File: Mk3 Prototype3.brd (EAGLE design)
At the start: 121.6 x 70 mm, 152 parts, among them IC1 TPD3E001DRL, IC2 TPS62082, IC3 STM32F401V, IC4 BQ24092, IC6 CC3100MOD, IC7 BQ2970, IC8 LSM6DS3, IC9 LIS3MDL, J1 ZX62-AB-5PA(11), J2 ER-CON50HT-1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

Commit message: Rework entier power section layout on schematic
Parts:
- JP3: value (none) -> JST PH 2mm
- R32: value DNP (0) -> DNP (0603/0R/5%)
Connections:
- net N$16 renamed VABT_SWTICHED
- net N$57 renamed VBAT_NEG
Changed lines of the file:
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@@
 <attribute name="FARNELL" value="1217769" x="16.2" y="24.8" size="1.778" layer="27" rot="R270" display="off"/>
 </element>
-<element name="JP3" library="TiLDA Mk3 Parts" package="JST-2-SMD" value="" x="47" y="58.8" smashed="yes" rot="MR0">
+<element name="JP3" library="TiLDA Mk3 Parts" package="JST-2-SMD" value="JST PH 2mm" x="47" y="58.8" smashed="yes" rot="MR0">
 <attribute name="NAME" x="48.17" y="61.97" size="1.016" layer="26" font="vector" ratio="14" rot="MR0"/>
 <attribute name="VALUE" x="48.27" y="58.8" size="0.4064" layer="28" rot="MR0"/>
@@
 </element>
 <element name="U2" library="TiLDA Mk3 Parts" package="ER-TFT024-3" value="ER-TFT024-3" x="35.2" y="19.6"/>
-<element name="R32" library="TiLDA Mk3 Parts" package="C0603K-SMALL" value="DNP (0)" x="49.6" y="52.2" smashed="yes" rot="MR90">
+<element name="R32" library="TiLDA Mk3 Parts" package="C0603K-SMALL" value="DNP (0603/0R/5%)" x="49.6" y="52.2" smashed="yes" rot="MR90">
 <attribute name="NAME" x="47.95" y="50.1" size="1.016" layer="26" ratio="14" rot="MR90"/>
 <attribute name="VALUE" x="47.95" y="51.4" size="1.016" layer="28" rot="MR90"/>
@@
 <wire x1="52.2" y1="54.725" x2="52.2" y2="54.625" width="0.2" layer="16"/>
 </signal>
-<signal name="N$57">
+<signal name="VBAT_NEG">
 <contactref element="JP3" pad="1"/>
 <contactref element="IC7" pad="4"/>
@@
 <wire x1="46.92605" y1="24.8" x2="52.67395" y2="24.8" width="0.2" layer="16"/>
 </signal>
-<signal name="N$16">
+<signal name="VABT_SWTICHED">
 <contactref element="Q2" pad="3"/>
 <contactref element="Q1" pad="6"/>
@@
 <wire x1="24.999025" y1="44.171975" x2="23.47" y2="45.701" width="0.2" layer="16"/>
 </signal>
+<signal name="FRAME1">
+</signal>
 </signals>

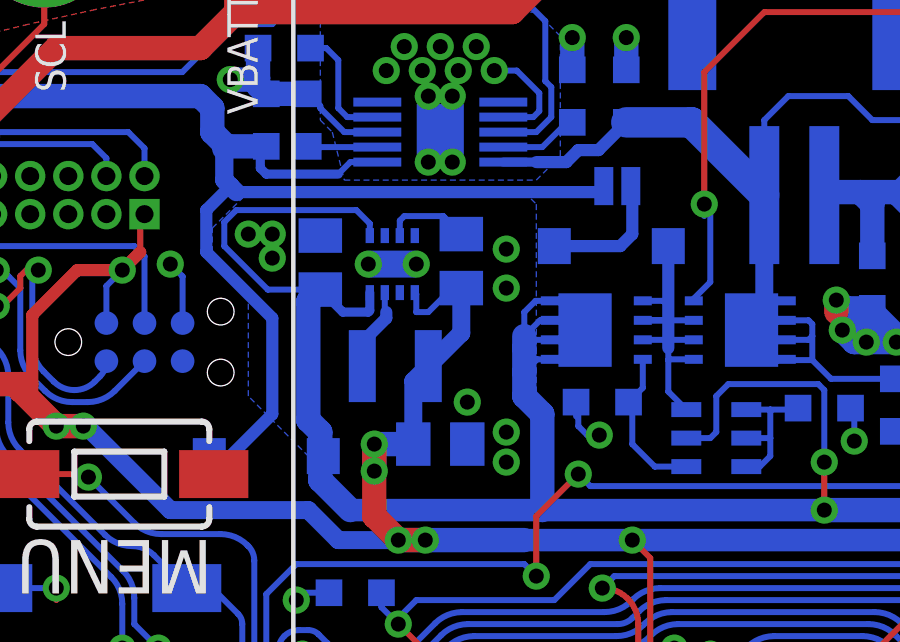
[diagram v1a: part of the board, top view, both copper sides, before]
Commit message: changing 4R7 -> 12R, more schematic tidying
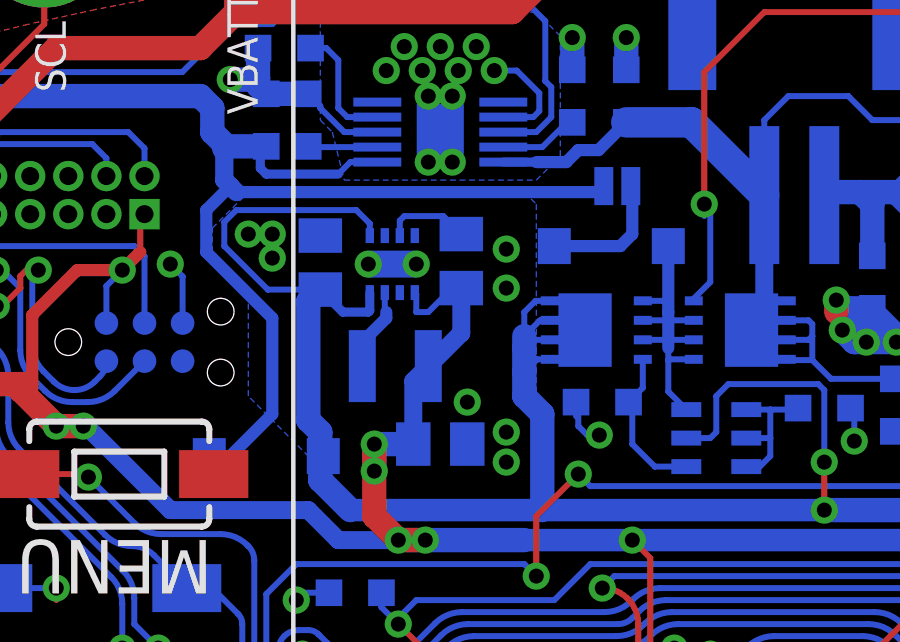
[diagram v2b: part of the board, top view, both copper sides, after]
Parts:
- R11: value DNP / 0603/100K/5% -> DNP
- R44, R47, R48, R49: value 0603/4R7/5% -> 0603/12R/5%
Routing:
- net VABT_SWTICHED: track 13.3 -> 12.5 mm
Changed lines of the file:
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@@
 <attribute name="NAME" x="29.411" y="15.9015" size="1.016" layer="26" font="vector" ratio="14" rot="MR180"/>
 </element>
-<element name="R11" library="TiLDA Mk3 Parts" package="C0603K-SMALL" value="DNP / 0603/100K/5%" x="31.5" y="10.65" smashed="yes" rot="MR0">
+<element name="R11" library="TiLDA Mk3 Parts" package="C0603K-SMALL" value="DNP" x="31.5" y="10.65" smashed="yes" rot="MR0">
 <attribute name="NAME" x="30.111" y="9.9515" size="1.016" layer="26" font="vector" ratio="14" rot="MR180"/>
 <variant name="L4" populate="no"/>
@@
 <variant name="L4" populate="no"/>
 </element>
-<element name="R47" library="TiLDA Mk3 Parts" package="C0603K-SMALL" value="0603/4R7/5%" x="69.6" y="59.2" smashed="yes" rot="MR270">
+<element name="R47" library="TiLDA Mk3 Parts" package="C0603K-SMALL" value="0603/12R/5%" x="69.6" y="59.2" smashed="yes" rot="MR270">
 <attribute name="NAME" x="69.05" y="54.8" size="1.016" layer="26" font="vector" ratio="14" rot="MR90"/>
 <attribute name="FARNELL" value="9331280" x="69.6" y="59.2" size="1.778" layer="28" rot="MR270" display="off"/>
 <attribute name="FARNELL_REEL" value="2130678" x="69.6" y="59.2" size="1.778" layer="28" rot="MR270" display="off"/>
 </element>
-<element name="R48" library="TiLDA Mk3 Parts" package="C0603K-SMALL" value="0603/4R7/5%" x="71.2" y="59.2" smashed="yes" rot="MR270">
+<element name="R48" library="TiLDA Mk3 Parts" package="C0603K-SMALL" value="0603/12R/5%" x="71.2" y="59.2" smashed="yes" rot="MR270">
 <attribute name="NAME" x="70.65" y="54.8" size="1.016" layer="26" font="vector" ratio="14" rot="MR90"/>
 <attribute name="FARNELL" value="9331280" x="71.2" y="59.2" size="1.778" layer="28" rot="MR270" display="off"/>
 <attribute name="FARNELL_REEL" value="2130678" x="71.2" y="59.2" size="1.778" layer="28" rot="MR270" display="off"/>
 </element>
-<element name="R49" library="TiLDA Mk3 Parts" package="C0603K-SMALL" value="0603/4R7/5%" x="72.8" y="59.2" smashed="yes" rot="MR270">
+<element name="R49" library="TiLDA Mk3 Parts" package="C0603K-SMALL" value="0603/12R/5%" x="72.8" y="59.2" smashed="yes" rot="MR270">
 <attribute name="NAME" x="72.25" y="54.8" size="1.016" layer="26" font="vector" ratio="14" rot="MR90"/>
 <attribute name="FARNELL" value="9331280" x="72.8" y="59.2" size="1.778" layer="28" rot="MR270" display="off"/>
@@
 <attribute name="NAME" x="61.895" y="54.0524" size="1.016" layer="26" font="vector" ratio="14" rot="MR90"/>
 </element>
-<element name="R44" library="TiLDA Mk3 Parts" package="C0603K-SMALL" value="0603/4R7/5%" x="74.4" y="59.2" smashed="yes" rot="MR270">
+<element name="R44" library="TiLDA Mk3 Parts" package="C0603K-SMALL" value="0603/12R/5%" x="74.4" y="59.2" smashed="yes" rot="MR270">
 <attribute name="NAME" x="73.85" y="54.8" size="1.016" layer="26" font="vector" ratio="14" rot="MR90"/>
 <attribute name="FARNELL" value="9331280" x="74.4" y="59.2" size="1.778" layer="28" rot="MR270" display="off"/>
@@
 <wire x1="28.075" y1="56.725" x2="29.4" y2="56.725" width="0.8128" layer="16"/>
 <wire x1="28.075" y1="56.725" x2="28" y2="56.65" width="0.8128" layer="16"/>
-<contactref element="SJ1" pad="2"/>
 <wire x1="2.4" y1="39.2" x2="2.4" y2="20" width="0.8128" layer="1"/>
 <wire x1="40.45" y1="55.2" x2="28.4" y2="55.2" width="0.4064" layer="16"/>
@@
 <wire x1="8.8" y1="9.2" x2="9.97" y2="9.2" width="0.8128" layer="1"/>
 <wire x1="9.97" y1="9.2" x2="10" y2="9.23" width="0.8128" layer="1"/>
-<contactref element="D3" pad="A"/>
 <wire x1="29.6" y1="51" x2="29.6" y2="47.8" width="0.4064" layer="16"/>
-<wire x1="27.5" y1="46.4" x2="28.2" y2="46.4" width="0.4064" layer="16"/>
 <wire x1="28.2" y1="46.4" x2="29.6" y2="47.8" width="0.4064" layer="16"/>
 <wire x1="16.8" y1="8.2" x2="16.7" y2="8.3" width="0.2" layer="16"/>
@@
 <wire x1="21.3" y1="5.425" x2="20.275" y2="4.4" width="0.2" layer="16"/>
 <wire x1="20.275" y1="4.4" x2="20" y2="4.4" width="0.2" layer="16"/>
-<wire x1="40.45" y1="55.2" x2="40.65" y2="55.4" width="0.4064" layer="16"/>
+<contactref element="SJ1" pad="2"/>
+<contactref element="D3" pad="A"/>
+<wire x1="40.45" y1="55.2" x2="40.65" y2="55.2" width="0.2" layer="16"/>
+<wire x1="40.65" y1="55.2" x2="40.65" y2="55.4" width="0.2" layer="16"/>
+<wire x1="28.2" y1="46.4" x2="27.5" y2="46.4" width="0.4064" layer="16"/>
 </signal>
 <signal name="N$6">
@@
 <contactref element="Q2" pad="1"/>
 <contactref element="Q2" pad="2"/>
-<contactref element="Q6" pad="3"/>
-<contactref element="Q6" pad="2"/>
-<contactref element="Q6" pad="1"/>
-<wire x1="41.95" y1="50.925" x2="43.65" y2="50.925" width="0.2" layer="16"/>
 <wire x1="41.95" y1="51.575" x2="42.625" y2="51.575" width="0.2" layer="16"/>
 <wire x1="42.625" y1="51.575" x2="42.8" y2="51.4" width="0.2" layer="16"/>
-<wire x1="42.8" y1="51.4" x2="42.8" y2="50.8" width="0.2" layer="16"/>
+<wire x1="42.8" y1="51.4" x2="42.8" y2="51.2" width="0.2" layer="16"/>
+<wire x1="42.8" y1="50.925" x2="42.8" y2="50.8" width="0.2" layer="16"/>
 <wire x1="42.8" y1="50.8" x2="42.8" y2="50.4" width="0.2" layer="16"/>
-<wire x1="42.8" y1="50.4" x2="42.8" y2="50.2" width="0.2" layer="16"/>
+<wire x1="42.8" y1="50.4" x2="42.8" y2="50.275" width="0.2" layer="16"/>
 <wire x1="42.8" y1="50.2" x2="42.8" y2="50" width="0.2" layer="16"/>
 <wire x1="42.8" y1="50" x2="42.8" y2="49.6" width="0.2" layer="16"/>
-<wire x1="43.65" y1="50.275" x2="42.875" y2="50.275" width="0.2" layer="16"/>
 <wire x1="42.875" y1="50.275" x2="42.8" y2="50.2" width="0.2" layer="16"/>
 <wire x1="41.95" y1="50.275" x2="42.675" y2="50.275" width="0.2" layer="16"/>
 <wire x1="42.675" y1="50.275" x2="42.8" y2="50.4" width="0.2" layer="16"/>
-<wire x1="43.65" y1="49.625" x2="42.825" y2="49.625" width="0.2" layer="16"/>
 <wire x1="42.825" y1="49.625" x2="42.8" y2="49.6" width="0.2" layer="16"/>
 <wire x1="41.95" y1="50.925" x2="42.675" y2="50.925" width="0.2" layer="16"/>
 <wire x1="42.675" y1="50.925" x2="42.8" y2="50.8" width="0.2" layer="16"/>
-<wire x1="42.8" y1="53.4" x2="42.8" y2="50" width="0.4064" layer="16"/>
+<wire x1="42.8" y1="53.4" x2="42.8" y2="51.2" width="0.4064" layer="16"/>
 <contactref element="D2" pad="A"/>
+<wire x1="42.8" y1="51.2" x2="42.8" y2="50" width="0.4064" layer="16"/>
 <wire x1="42.8" y1="49.6" x2="42.8" y2="48.55" width="0.2" layer="16"/>
 <wire x1="42.8" y1="48.55" x2="43.4" y2="47.95" width="0.2" layer="16"/>
+<contactref element="Q6" pad="3"/>
+<contactref element="Q6" pad="2"/>
+<contactref element="Q6" pad="1"/>
+<wire x1="43.65" y1="50.925" x2="42.8" y2="50.925" width="0.2" layer="16"/>
+<wire x1="42.8" y1="50.925" x2="42.8" y2="51.2" width="0.2" layer="16"/>
+<wire x1="43.65" y1="50.275" x2="42.8" y2="50.275" width="0.2" layer="16"/>
+<wire x1="42.8" y1="50.275" x2="42.8" y2="50.2" width="0.2" layer="16"/>
+<wire x1="43.65" y1="49.625" x2="42.825" y2="49.625" width="0.2" layer="16"/>
 </signal>
 <signal name="BTN_MENU">

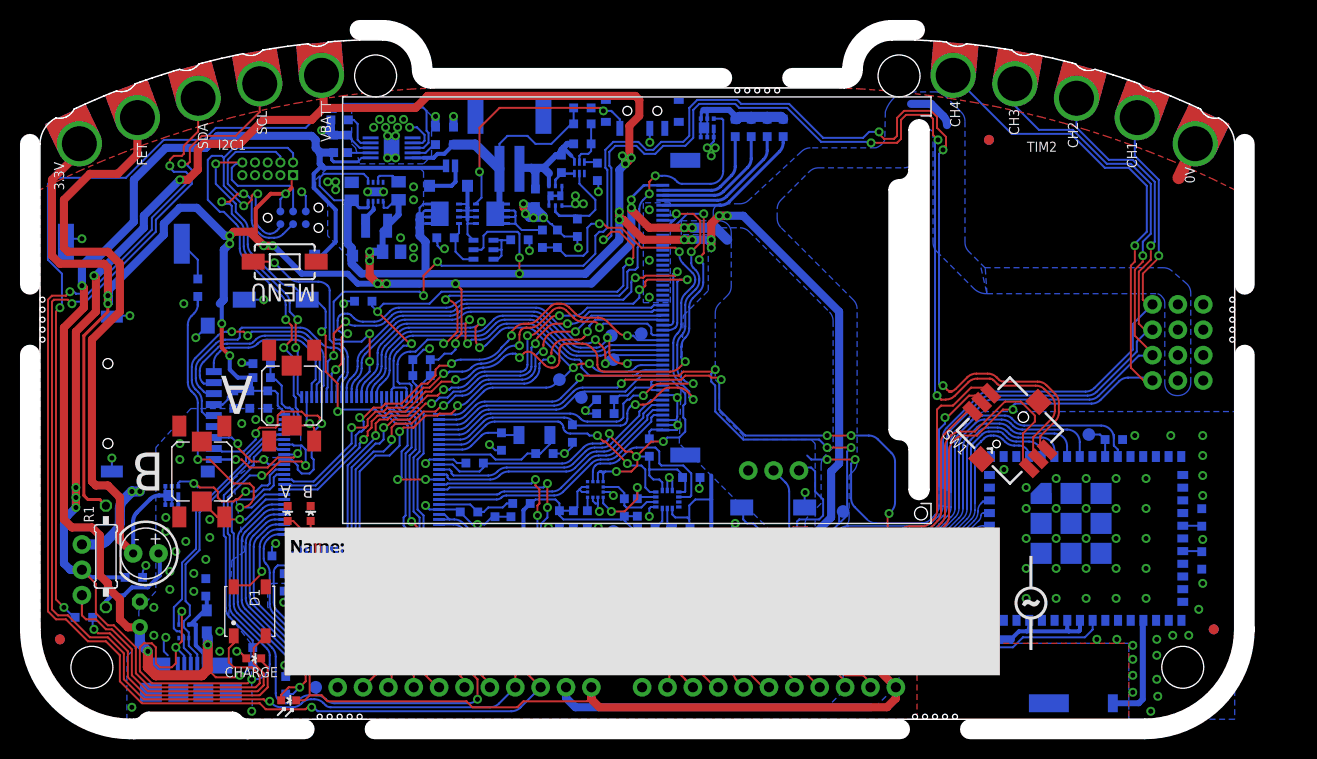
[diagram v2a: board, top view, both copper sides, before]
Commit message: Front silk and move joystick over 2mm
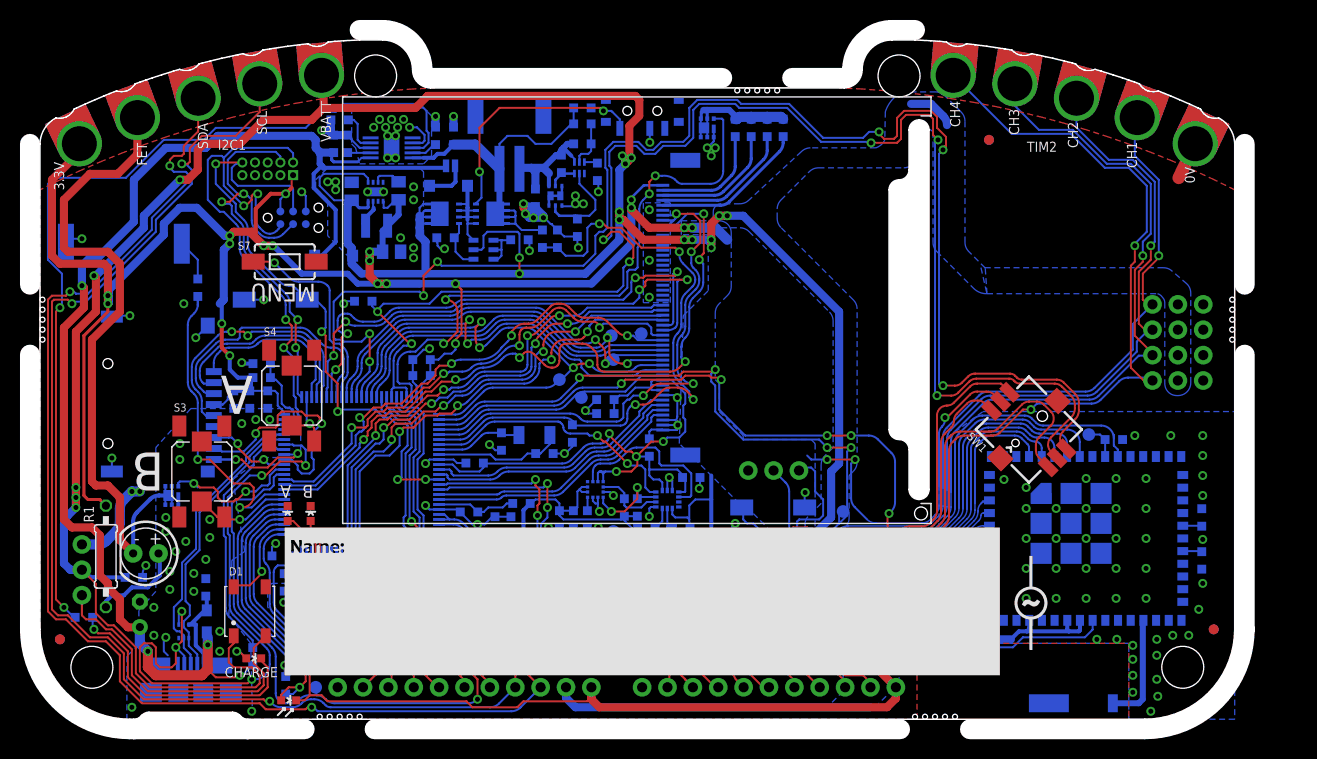
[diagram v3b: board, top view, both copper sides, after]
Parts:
- moved SW1 1.90 mm to (99.0, 29.0)
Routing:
- net JOY_DOWN: track 107.2 -> 110.1 mm
- net +3V3: track 545.7 -> 547.7 mm
- net BOOT0: track 147.3 -> 149.0 mm
- net JOY_LEFT: track 109.3 -> 111.0 mm
- net JOY_UP: track 120.0 -> 121.0 mm
- net JOY_RIGHT: track 146.6 -> 147.3 mm
- net CC_HIB: track 128.8 -> 129.4 mm
- net GND: vias 155 -> 154

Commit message: π to a 1000 digits
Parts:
- moved U$5 25.5 mm to (124.2, 16.6)
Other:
- board text added: "@CharlesYarnold"
- board text added: "@dpslwk"
- board text added: "@drrk"
- board text added: "@gmjhowe"
- board text added: "@jonty"
- board text added: "@marekventur"
- board text added: "@marksteward"
- board text added: "@russss"
- board text added: "@thinkl33t"
- board text added: "Brought to you by:"
- board text added: "MKπ"
- board text added: "TiLDA"
- board text added: "mattbrejza"
- board text added: "v3. 1415926535 8979323846 2643383279 5028841971 6939937510 5820974944 5923078164 0628620899 8628034825 3421170679 8214808651 3282306647 0938446095 5058223172 5359408128 4811174502 8410270193 8521105559 6446229489 5493038196 4428810975 6659334461 2847564823 3786783165 2712019091 4564856692 3460348610 4543266482 1339360726 0249141273 7245870066 0631558817 4881520920 9628292540 9171536436 7892590360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"
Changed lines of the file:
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@@
 <text x="44.6" y="4.8" size="1.016" layer="22" font="vector" ratio="14" rot="MR90">DAC</text>
 <text x="27" y="4.1" size="1.016" layer="22" font="vector" ratio="14" rot="MR90">!HIB</text>
+<wire x1="-0.4" y1="0" x2="0.4" y2="0" width="0.15" layer="21"/>
+<wire x1="0" y1="0.4" x2="0" y2="-0.4" width="0.15" layer="21"/>
+<text x="152.2" y="2" size="3.5" layer="22" font="vector" ratio="20" rot="MR0">TiLDA</text>
+<text x="137.1" y="2" size="1.9304" layer="22" font="vector" ratio="15" rot="MR0">MKπ</text>
+<text x="71" y="47" size="1.27" layer="21" font="vector" ratio="15">Brought to
+you by:</text>
+<text x="71" y="43.5" size="1.27" layer="21" font="vector" ratio="15">@dpslwk</text>
+<text x="71" y="41" size="1.27" layer="21" font="vector" ratio="15">@thinkl33t</text>
+<text x="71" y="33.5" size="1.27" layer="21" font="vector" ratio="15">@jonty</text>
+<text x="71" y="20" size="1.27" layer="21" font="vector" ratio="15">@CharlesYarnold</text>
+<text x="71" y="36" size="1.27" layer="21" font="vector" ratio="15">@drrk</text>
+<text x="71" y="38.5" size="1.27" layer="21" font="vector" ratio="15">mattbrejza  </text>
+<text x="71" y="26" size="1.27" layer="21" font="vector" ratio="15">@marekventur</text>
+<text x="71" y="31" size="1.27" layer="21" font="vector" ratio="15">@russss</text>
+<text x="71" y="28.5" size="1.27" layer="21" font="vector" ratio="15">@gmjhowe</text>
+<text x="71" y="22.5" size="1.27" layer="21" font="vector" ratio="15">@marksteward</text>
+<text x="30.6" y="20" size="1.016" layer="21" font="vector" ratio="15" rot="R90" align="top-left">v3.
+1415926535 8979323846 2643383279 5028841971
+6939937510 5820974944 5923078164 0628620899
+8628034825 3421170679 8214808651 3282306647
+0938446095 5058223172 5359408128 4811174502
+8410270193 8521105559 6446229489 5493038196
+4428810975 6659334461 2847564823 3786783165
+2712019091 4564856692 3460348610 4543266482
+1339360726 0249141273 7245870066 0631558817
+4881520920 9628292540 9171536436 7892590360
+0113305305 4882046652 1384146951 9415116094
+3305727036 5759591953 0921861173 8193261179
+3105118548 0744623799 6274956735 1885752724
+8912279381 8301194912 9833673362 4406566430
+8602139494 6395224737 1907021798 6094370277
+0539217176 2931767523 8467481846 7669405132
+0005681271 4526356082 7785771342 7577896091
+7363717872 1468440901 2249534301 4654958537
+1050792279 6892589235 4201995611 2129021960
+8640344181 5981362977 4771309960 5187072113
+4999999837 2978049951 0597317328 1609631859
+5024459455 3469083026 4252230825 3344685035
+2619311881 7101000313 7838752886 5875332083
+8142061717 7669147303 5982534904 2875546873
+1159562863 8823537875 9375195778 1857780532
+1712268066 1300192787 6611195909 216420198</text>
+<text x="71.2" y="55" size="3.5" layer="21" font="vector" ratio="20">TiLDA</text>
+<text x="71.1" y="52" size="1.9304" layer="21" font="vector" ratio="15">MKπ</text>
 </plain>
 <attributes>
@@
 </element>
 <element name="U$1" library="TiLDA Mk3 Parts" package="NAME_AREA" value="" x="24.625" y="19.125"/>
-<element name="U$5" library="TiLDA Mk3 Parts" package="EMFLOGO1" value="" x="99.2" y="11.6"/>
+<element name="U$5" library="TiLDA Mk3 Parts" package="EMFLOGO1" value="" x="124.2" y="16.6"/>
 <element name="R18" library="TiLDA Mk3 Parts" package="C0603K-SMALL" value="DNP (0603/10k/5%)" x="60.7" y="19.1" smashed="yes" rot="MR180">
 <attribute name="NAME" x="61.9" y="17.55" size="1.016" layer="26" font="vector" ratio="14" rot="MR0"/>
